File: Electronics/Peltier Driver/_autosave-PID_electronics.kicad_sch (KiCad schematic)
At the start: 21 parts, among them J1 Conn_01x05, J2 Conn_01x03, Q3 2N7000, U1 LF412

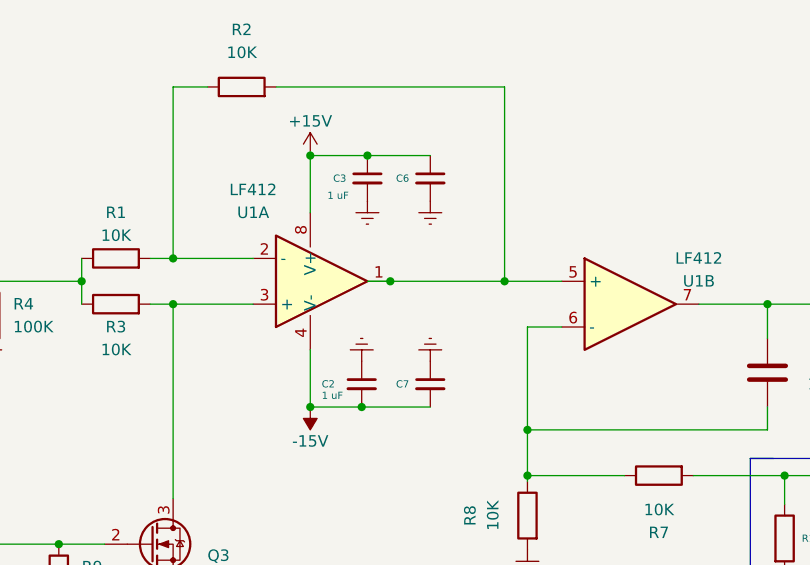
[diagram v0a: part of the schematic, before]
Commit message: Added additional optional bypass capacitors
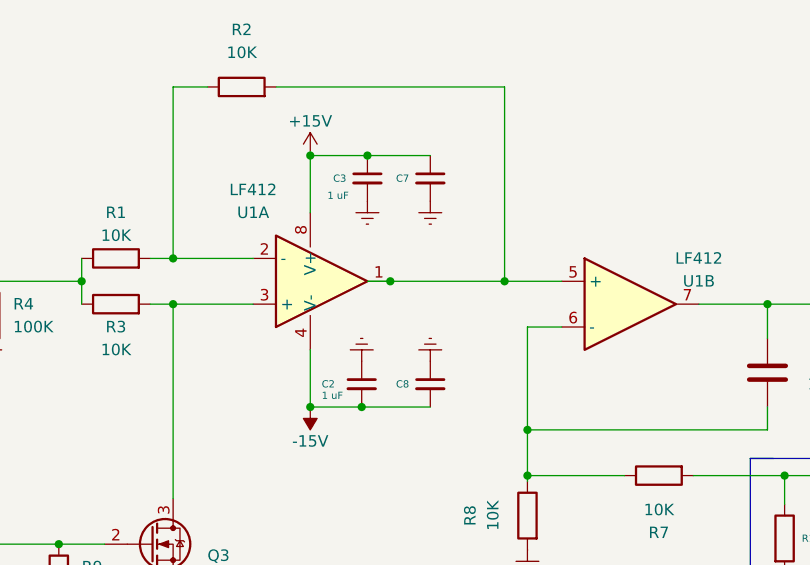
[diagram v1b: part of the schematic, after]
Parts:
- renumbered C6 to C7, C7 to C8
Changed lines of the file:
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@@
   (symbol (lib_id "Device:C_Small") (at 163.83 60.96 0) (mirror y) (unit 1)
     (in_bom yes) (on_board yes)
-    (property "Reference" "C6" (id 0) (at 160.02 60.96 0)
+    (property "Reference" "C7" (id 0) (at 160.02 60.96 0)
       (effects (font (size 0.8 0.8)) (justify right))
     )
@@
   (symbol (lib_id "Device:C_Small") (at 163.83 83.82 0) (unit 1)
     (in_bom yes) (on_board yes)
-    (property "Reference" "C7" (id 0) (at 160.02 83.82 0)
+    (property "Reference" "C8" (id 0) (at 160.02 83.82 0)
       (effects (font (size 0.8 0.8)) (justify left))
     )
@@
       (reference "C5") (unit 1) (value "1000 uF") (footprint "Capacitor_THT:CP_Radial_D10.0mm_P5.00mm")
     )
-    (path "/29bc48cf-d8fe-4214-b2d7-759437472a93"
-      (reference "C6") (unit 1) (value "C_Small") (footprint "Capacitor_THT:C_Axial_L3.8mm_D2.6mm_P7.50mm_Horizontal")
-    )
     (path "/8ea27319-6561-48d0-833e-434a565ff3b2"
       (reference "C6") (unit 1) (value "C_Small") (footprint "Capacitor_THT:CP_Radial_D10.0mm_P5.00mm")
     )
+    (path "/29bc48cf-d8fe-4214-b2d7-759437472a93"
+      (reference "C7") (unit 1) (value "C_Small") (footprint "Capacitor_THT:C_Axial_L3.8mm_D2.6mm_P7.50mm_Horizontal")
+    )
     (path "/dbe3ed1d-1e50-4ccd-ba3e-6e66d24024b4"
-      (reference "C7") (unit 1) (value "C_Small") (footprint "Capacitor_THT:C_Axial_L3.8mm_D2.6mm_P7.50mm_Horizontal")
+      (reference "C8") (unit 1) (value "C_Small") (footprint "Capacitor_THT:C_Axial_L3.8mm_D2.6mm_P7.50mm_Horizontal")
     )
     (path "/eecd43dc-9458-46d0-afaa-bc2f0fdbe268"
